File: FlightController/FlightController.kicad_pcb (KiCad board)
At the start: 2 copper layers, 65 x 30 mm, 5 parts, among them J1 GPIO

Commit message: Place components
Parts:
- added BZ1: CEM-1201S, Buzzer_Beeper:MagneticBuzzer_ProSignal_ABT-410-RC, F.Cu at (180.0, 215.0)
- added C1: 0µ1, Capacitor_SMD:C_0805_2012Metric_Pad1.18x1.45mm_HandSolder, F.Cu at (188.5, 231.5)
- added C10: 0µ1, Capacitor_SMD:C_0805_2012Metric_Pad1.18x1.45mm_HandSolder, F.Cu at (217.5, 196.8)
- added C11: 22µ, Capacitor_SMD:C_0805_2012Metric_Pad1.18x1.45mm_HandSolder, F.Cu at (222.0, 203.0)
- added C2: 0µ1, Capacitor_SMD:C_0805_2012Metric_Pad1.18x1.45mm_HandSolder, F.Cu at (216.5, 227.0)
- added C3: 22µ, Capacitor_SMD:C_0805_2012Metric_Pad1.18x1.45mm_HandSolder, F.Cu at (221.0, 199.0)
- added C4: 22µ, Capacitor_SMD:C_0805_2012Metric_Pad1.18x1.45mm_HandSolder, F.Cu at (214.0, 201.0)
- added C5: 22µ, Capacitor_SMD:C_0805_2012Metric_Pad1.18x1.45mm_HandSolder, F.Cu at (212.0, 201.0)
- added C6: 22µ, Capacitor_SMD:C_0805_2012Metric_Pad1.18x1.45mm_HandSolder, F.Cu at (210.0, 201.0)
- added C7: 0µ1, Capacitor_SMD:C_0805_2012Metric_Pad1.18x1.45mm_HandSolder, F.Cu at (218.0, 217.9)
- added C8: 10p, Capacitor_SMD:C_0805_2012Metric_Pad1.18x1.45mm_HandSolder, F.Cu at (214.0, 197.0)
- added C9: 1µ, Capacitor_SMD:C_0805_2012Metric_Pad1.18x1.45mm_HandSolder, F.Cu at (191.5, 189.5)
- added D1: 1N4148W, Diode_SMD:D_SOD-123, F.Cu at (215.5, 216.8)
- added D2: 1N4148W, Diode_SMD:D_SOD-123, F.Cu at (182.0, 197.5)
- added H1: MountingHole_Pad, MountingHole:MountingHole_3.2mm_M3_DIN965_Pad_TopBottom, F.Cu at (175.0, 170.0)
- added H2: MountingHole_Pad, MountingHole:MountingHole_3.2mm_M3_DIN965_Pad_TopBottom, F.Cu at (225.0, 170.0)
- added H3: MountingHole_Pad, MountingHole:MountingHole_3.2mm_M3_DIN965_Pad_TopBottom, F.Cu at (175.0, 230.0)
- added H4: MountingHole_Pad, MountingHole:MountingHole_3.2mm_M3_DIN965_Pad_TopBottom, F.Cu at (225.0, 230.0)
- added H5: MountingHole_Pad, MountingHole:MountingHole_2.2mm_M2_DIN965_Pad_TopBottom, F.Cu at (213.0, 207.0)
- added J2: USB_C_Receptacle_USB2.0_14P, Connector_USB:USB_C_Receptacle_HRO_TYPE-C-31-M-12, F.Cu at (174.0, 200.0)
- added J3: Conn_01x02, Connector_PinHeader_2.54mm:PinHeader_1x02_P2.54mm_Vertical, F.Cu at (225.0, 202.5)
- added J4: 60312002114503, Connector_Coaxial:SMA_Wurth_60312002114503_Vertical, F.Cu at (200.0, 170.0)
- added JP1: Power Save, Jumper:SolderJumper-3_P1.3mm_Bridged12_RoundedPad1.0x1.5mm, F.Cu at (217.5, 194.0)
- added L1: 1µH, Inductor_SMD:L_Coilcraft_XxL4020, F.Cu at (217.5, 205.5)
- added NT1: NetTie_2, NetTie:NetTie-2_SMD_Pad0.5mm, F.Cu at (220.5, 201.5)
- added NT2: NetTie_2, NetTie:NetTie-2_SMD_Pad0.5mm, F.Cu at (206.0, 198.0)
- added NT3: NetTie_2, NetTie:NetTie-2_SMD_Pad0.5mm, F.Cu at (189.5, 188.0)
- added Q1: Si2338DS, Package_TO_SOT_SMD:SOT-23, F.Cu at (192.5, 212.0)
- added Q2: SI2347DS, Package_TO_SOT_SMD:SOT-23, F.Cu at (207.5, 212.0)
- added R1: 10k, Resistor_SMD:R_0805_2012Metric_Pad1.20x1.40mm_HandSolder, F.Cu at (188.5, 227.5)
- added R10: 120k, Resistor_SMD:R_0805_2012Metric_Pad1.20x1.40mm_HandSolder, F.Cu at (186.5, 209.0)
- added R11: 5k1, Resistor_SMD:R_0805_2012Metric_Pad1.20x1.40mm_HandSolder, F.Cu at (182.5, 200.0)
- added R12: 5k1, Resistor_SMD:R_0805_2012Metric_Pad1.20x1.40mm_HandSolder, F.Cu at (182.5, 203.5)
- added R2: 100k, Resistor_SMD:R_0805_2012Metric_Pad1.20x1.40mm_HandSolder, F.Cu at (219.5, 225.0)
- added R3: 220k, Resistor_SMD:R_0805_2012Metric_Pad1.20x1.40mm_HandSolder, F.Cu at (219.5, 229.0)
- added R4: 10k, Resistor_SMD:R_0805_2012Metric_Pad1.20x1.40mm_HandSolder, F.Cu at (221.0, 215.0)
- added R5: 1M, Resistor_SMD:R_0805_2012Metric_Pad1.20x1.40mm_HandSolder, F.Cu at (210.0, 197.0)
- added R6: 10k, Resistor_SMD:R_0805_2012Metric_Pad1.20x1.40mm_HandSolder, F.Cu at (220.0, 218.0)
- added R7: 1M, Resistor_SMD:R_0805_2012Metric_Pad1.20x1.40mm_HandSolder, F.Cu at (208.0, 197.0)
- added R8: 180k, Resistor_SMD:R_0805_2012Metric_Pad1.20x1.40mm_HandSolder, F.Cu at (212.0, 197.0)
- added R9: 120k, Resistor_SMD:R_0805_2012Metric_Pad1.20x1.40mm_HandSolder, F.Cu at (218.0, 214.0)
- added SW1: SW_SPST, htl_smd:SW_Push_5.1mm_H1.5mm, F.Cu at (175.0, 190.0)
- added SW2: SW_SPST, Connector_PinHeader_2.54mm:PinHeader_1x02_P2.54mm_Vertical, F.Cu at (225.0, 215.0)
- added TP1: TestPoint, TestPoint:TestPoint_Pad_D1.0mm, F.Cu at (208.5, 190.0)
- added U1: BME680, Package_LGA:Bosch_LGA-8_3x3mm_P0.8mm_ClockwisePinNumbering, F.Cu at (200.0, 198.0)
- added U2: ESP32-S3-MINI-1, RF_Module:ESP32-S2-MINI-1, F.Cu at (200.0, 229.6)
- added U3: TPS63060, Package_SON:Texas_DSC0010J_ThermalVias, F.Cu at (217.6, 201.0)
- added U4: BME680, Package_LGA:Bosch_LGA-8_3x3mm_P0.8mm_ClockwisePinNumbering, F.Cu at (200.0, 205.0)
- added U5: NEO-M9N, RF_GPS:ublox_NEO, F.Cu at (200.0, 182.9)
- added U6: BME680, Package_LGA:Bosch_LGA-8_3x3mm_P0.8mm_ClockwisePinNumbering, F.Cu at (200.0, 212.0)
- J1: value GPIO -> Conn_01x06; footprint Connector_PinSocket_2.54mm:PinSocket_2x20_P2.54mm_Vertical -> Connector_PinHeader_2.54mm:PinHeader_1x06_P2.54mm_Vertical; moved to F.Cu
- moved J1 156.7 mm to (225.0, 179.4), turned to 0 degrees
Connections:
- J1 pad 1: +3V3 -> GND
- J1 pad 2: +5V -> CSB4
- J1 pad 3: /GPIO2/SDA1 -> MOSI
- J1 pad 4: +5V -> SCK
- J1 pad 5: /GPIO3/SCL1 -> MISO
- J1 pad 6: GND -> +3V3
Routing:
- added copper zone on B.Cu, net GND
- added copper zone on F.Cu, net GND
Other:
- board size 65 x 30 mm -> 60 x 70 mm
- board text added: "/\ UP"
- board text removed: "Extend PCB edge 0.5mm if using SMT header"
- board text removed: "PoE"

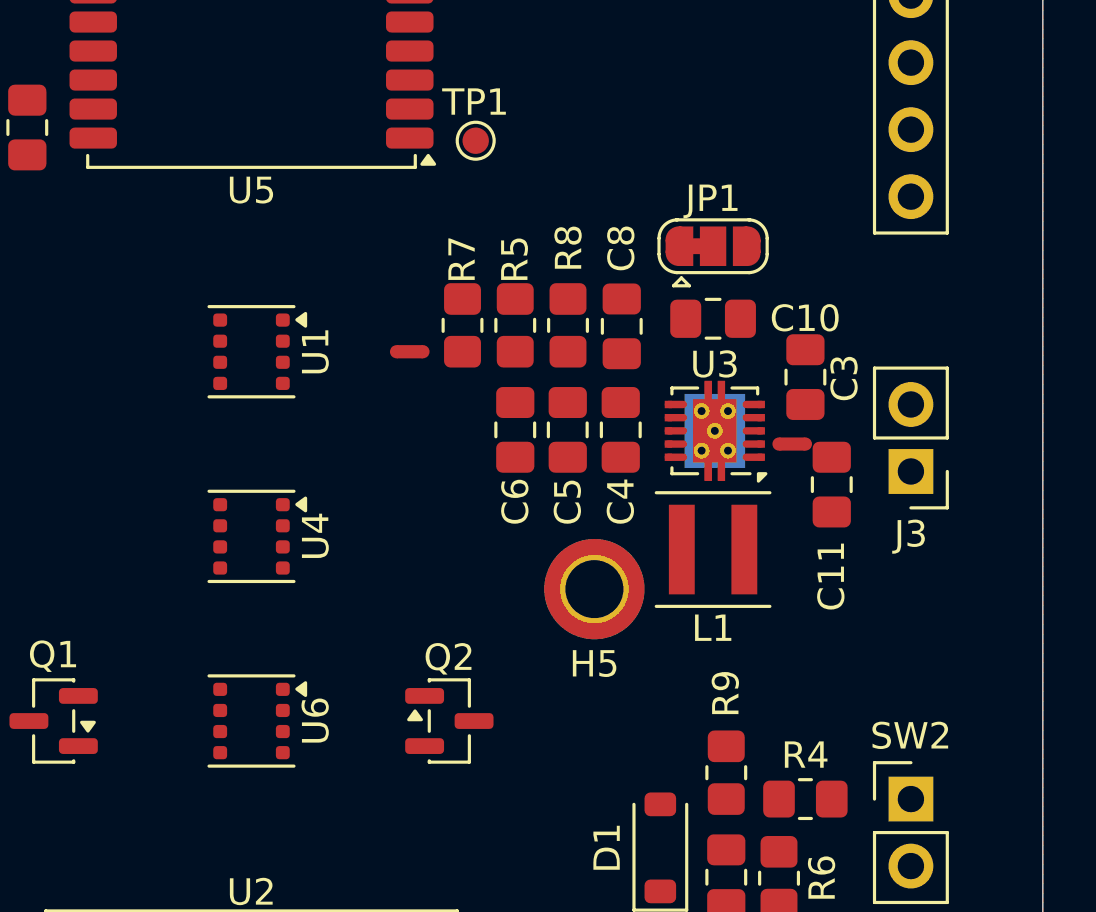
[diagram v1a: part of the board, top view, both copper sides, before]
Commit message: Add Battery Connector Footprint
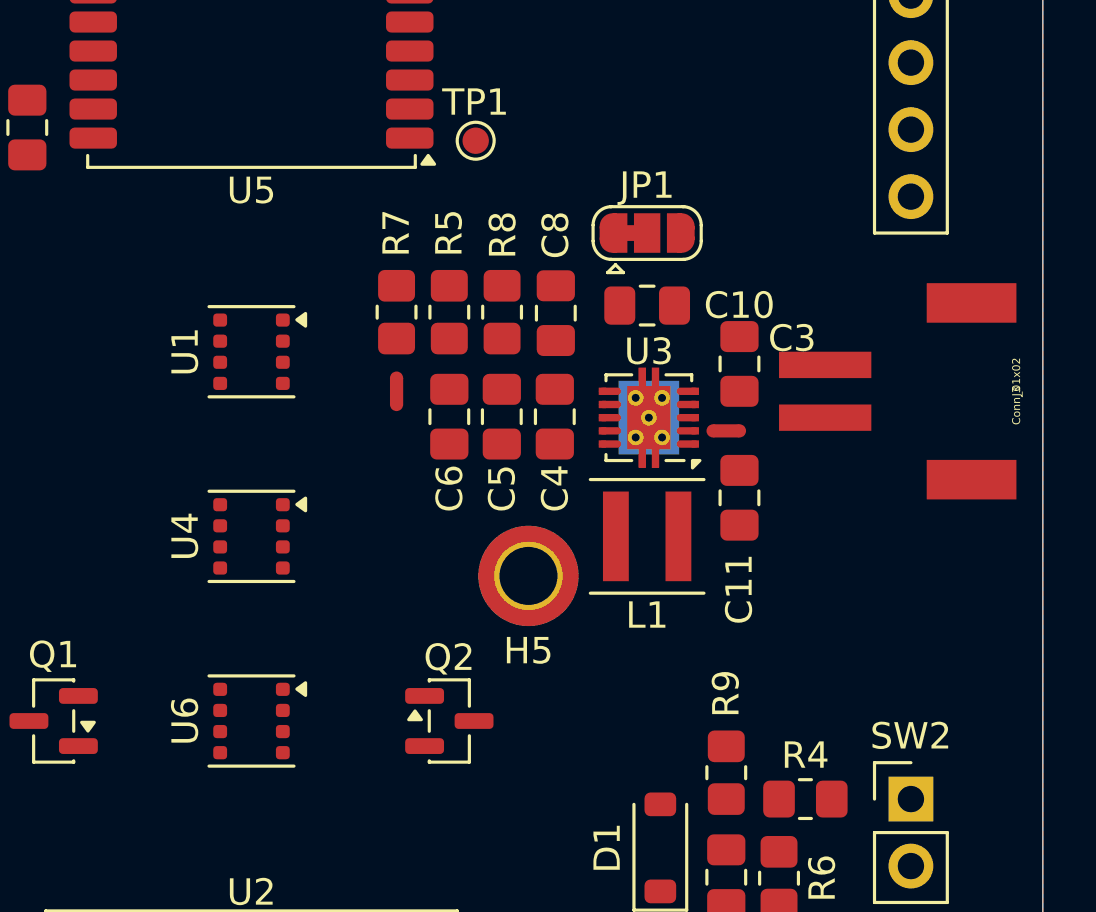
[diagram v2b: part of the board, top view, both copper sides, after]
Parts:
- J3: footprint Connector_PinHeader_2.54mm:PinHeader_1x02_P2.54mm_Vertical -> Connector_Battery:JST-PH-2
- moved J3 5.02 mm to (229.0, 199.5), turned to 90 degrees
- moved C11 3.54 mm to (218.5, 203.5)
- moved C10 2.55 mm to (215.0, 196.2)
- moved C3 2.55 mm to (218.5, 198.5)
- moved C4 2.55 mm to (211.5, 200.5)
- moved C5 2.55 mm to (209.5, 200.5)
- moved C6 2.55 mm to (207.5, 200.5)
- moved C8 2.55 mm to (211.5, 196.5)
- moved H5 2.55 mm to (210.5, 206.5)
- moved JP1 2.55 mm to (215.0, 193.5)
- moved L1 2.55 mm to (215.0, 205.0)
- moved NT1 2.55 mm to (218.0, 201.0)
- moved R5 2.55 mm to (207.5, 196.5)
- moved R7 2.55 mm to (205.5, 196.5)
- moved R8 2.55 mm to (209.5, 196.5)
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
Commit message: Fix wrong power symbol
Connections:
- NT3 pad 2: +3.3V -> +3V3
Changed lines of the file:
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@@
 		(capping no)
 		(filling no)
+		(zone_defaults)
 		(aux_axis_origin 100 100)
 		(grid_origin 100 100)
@@
 			(size 0.5 0.5)
 			(layers "F.Cu")
-			(net "+3.3V")
+			(net "+3V3")
 			(pinfunction "2_2")
 			(pintype "passive")

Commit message: route pcb
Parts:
- moved C1 0.50 mm to (188.0, 231.5)
- moved C4 0.50 mm to (211.0, 200.5)
- moved C6 0.50 mm to (207.0, 200.5)
- moved R1 0.50 mm to (188.0, 227.5)
- moved C5 0.49 mm to (209.0, 200.5)
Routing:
- net +3V3: track 0.00 -> 139.5 mm, vias 0 -> 9
- net +BATT: track 0.00 -> 120.0 mm, vias 0 -> 11
- net MOSI: track 0.00 -> 87.7 mm, vias 0 -> 6
- net MISO: track 0.00 -> 77.2 mm, vias 0 -> 4
- net SCK: track 0.00 -> 75.0 mm, vias 0 -> 4
- net Net-(SW1-B): track 0.00 -> 73.0 mm, vias 0 -> 4
- net CSB4: track 0.00 -> 70.0 mm, vias 0 -> 2
- net CSB3: track 0.00 -> 64.8 mm, vias 0 -> 2
- net PG: track 0.00 -> 60.7 mm, vias 0 -> 4
- net D-: track 0.00 -> 45.1 mm, vias 0 -> 4
- net D+: track 0.00 -> 40.5 mm, vias 0 -> 2
- net CSB0: track 0.00 -> 35.3 mm, vias 0 -> 4
- net CSB1: track 0.00 -> 31.6 mm, vias 0 -> 6
- net Net-(Q2-D): track 0.00 -> 22.2 mm, vias 0 -> 3
- net FAULT: track 0.00 -> 21.8 mm, vias 0 -> 2
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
